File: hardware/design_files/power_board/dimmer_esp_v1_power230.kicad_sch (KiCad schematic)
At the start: 4 parts, among them J1 Socket_1, J2 250VAC IN

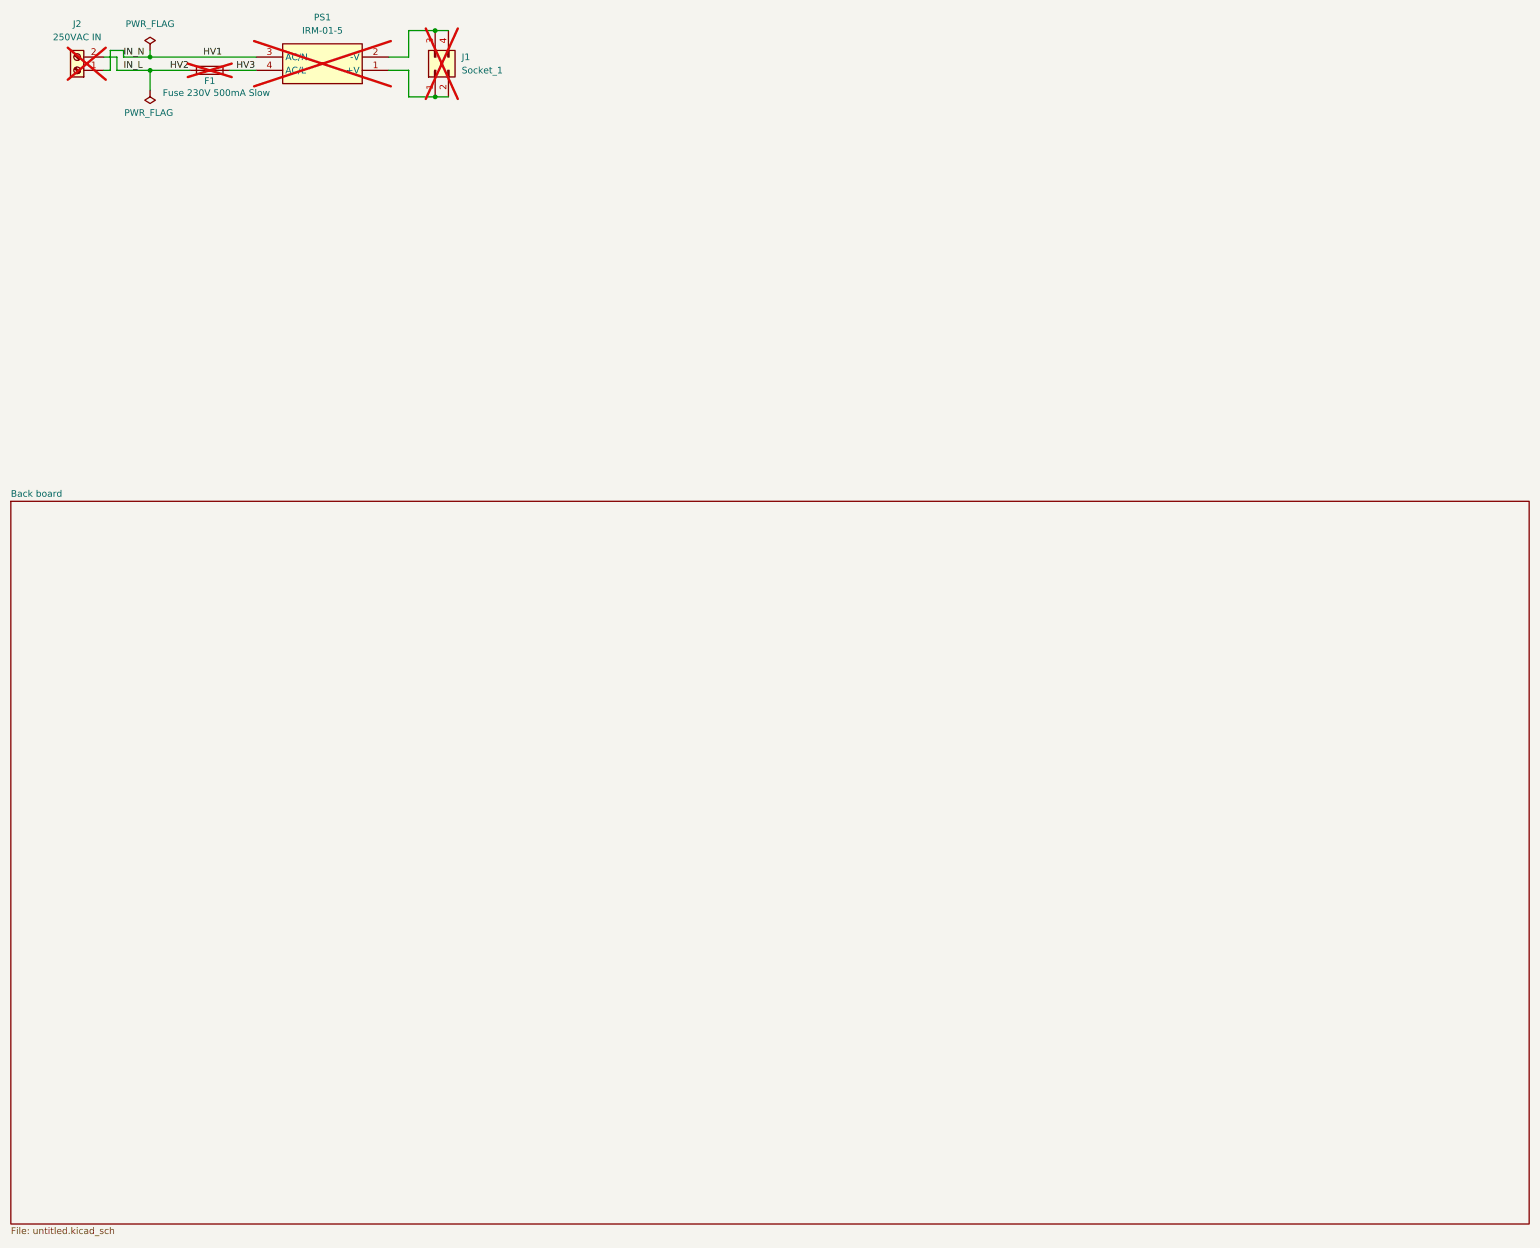
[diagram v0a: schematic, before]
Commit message: Remove unused second page from schematics
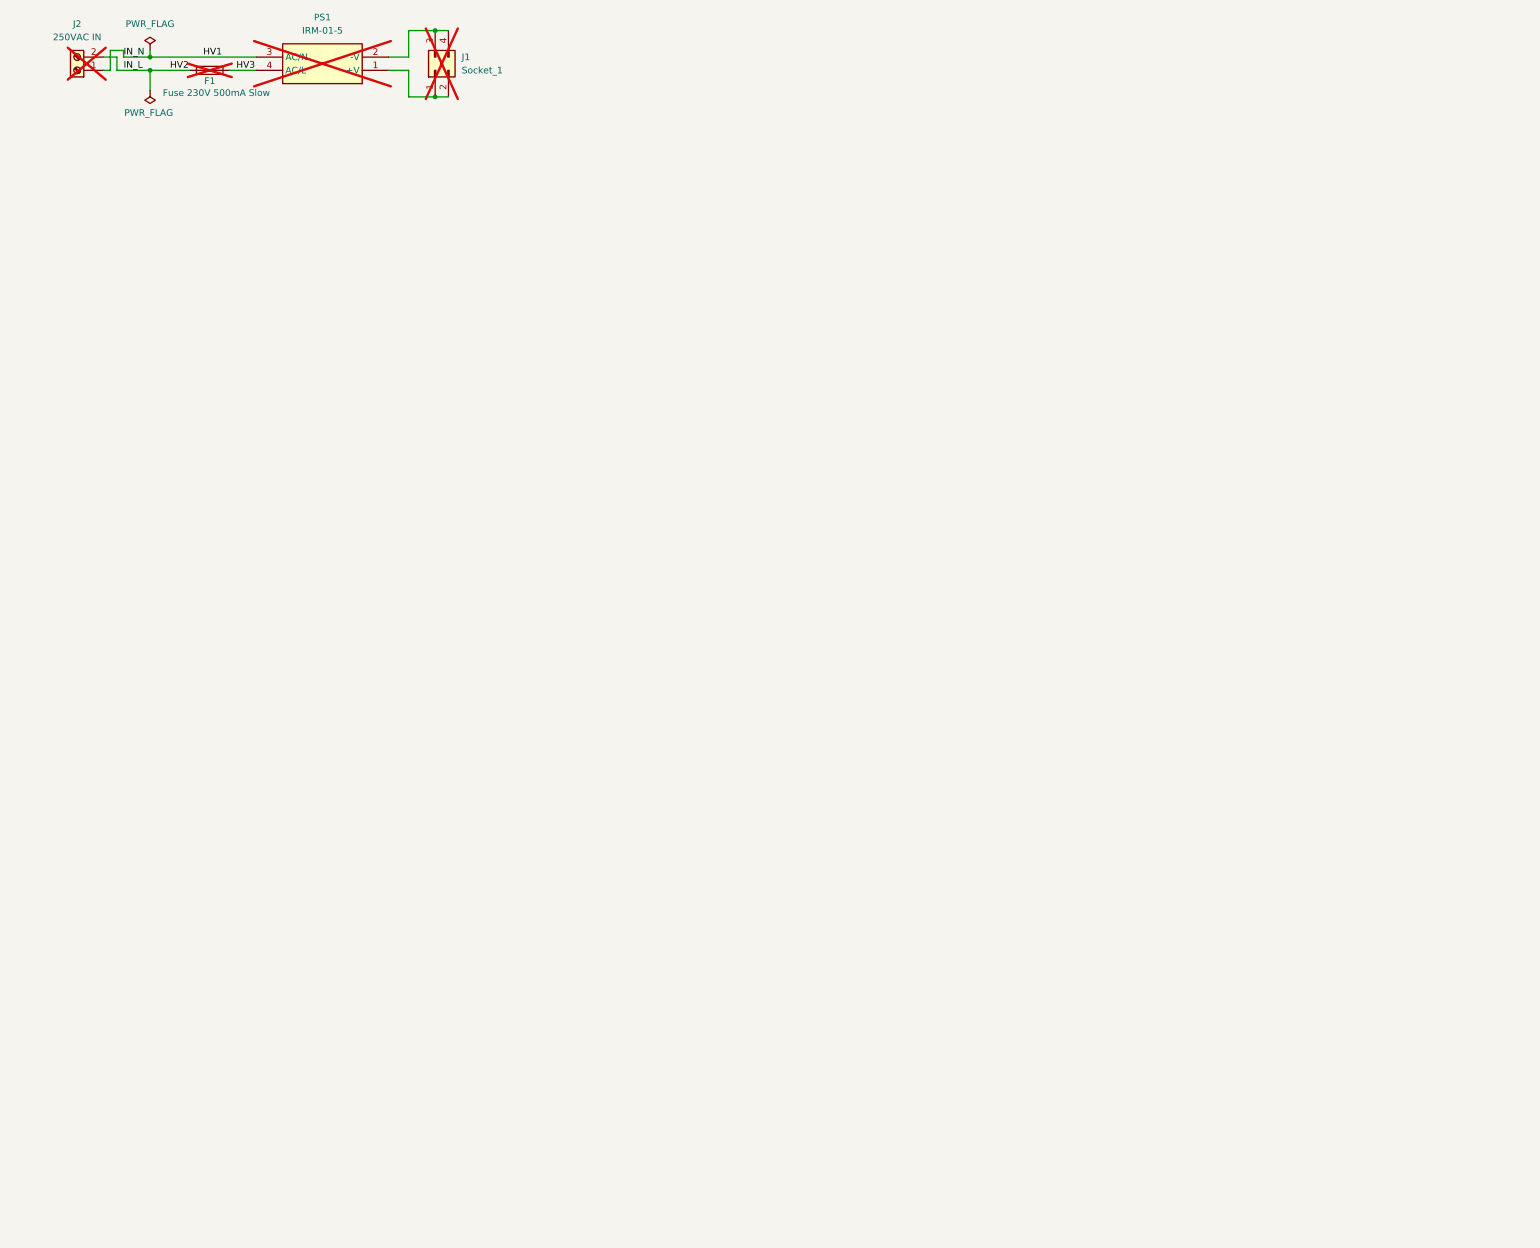
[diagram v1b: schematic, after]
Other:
- removed sheet Back board
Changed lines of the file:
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@@
-		)
-	)
-	(sheet
-		(at 8.89 236.22)
-		(size 290.83 138.43)
-		(fields_autoplaced yes)
-		(stroke
-			(width 0.1524)
-			(type solid)
-		)
-		(fill
-			(color 0 0 0 0.0000)
-		)
-		(property "Sheetname" "Back board"
-			(at 8.89 235.5084 0)
-			(effects
-				(font
-					(size 1.27 1.27)
-				)
-				(justify left bottom)
-			)
-		)
-		(property "Sheetfile" "untitled.kicad_sch"
-			(at 8.89 375.2346 0)
-			(effects
-				(font
-					(size 1.27 1.27)
-				)
-				(justify left top)
-			)
-		)
-		(instances
-			(project "dimmer_esp_v1_power230"
-				(path "/ddfcd425-273c-4c73-9404-db5c5faab60e"
-					(page "2")
-				)
-			)
 		)
 	)
